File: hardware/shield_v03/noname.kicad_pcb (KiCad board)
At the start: 2 copper layers, 42 parts, among them J1 GS2, J2 GS2, J3 GS2, J4 Conn_02x05, J5 Conn_02x05, P1 V_IN, P2 PINZA_1, P3 PINZA_2, P4 PINZA_3, P5 PINZA_4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

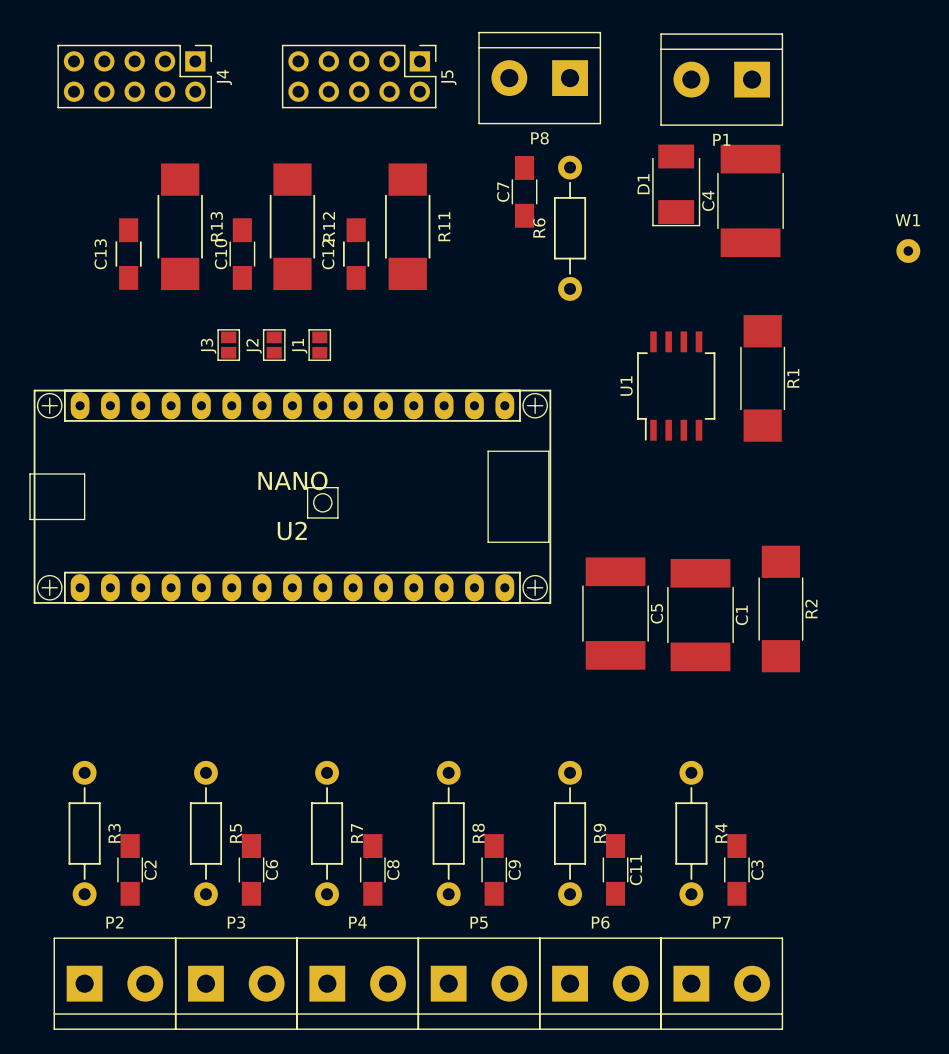
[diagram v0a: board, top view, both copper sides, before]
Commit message: hardware, rehubicacion de componentes
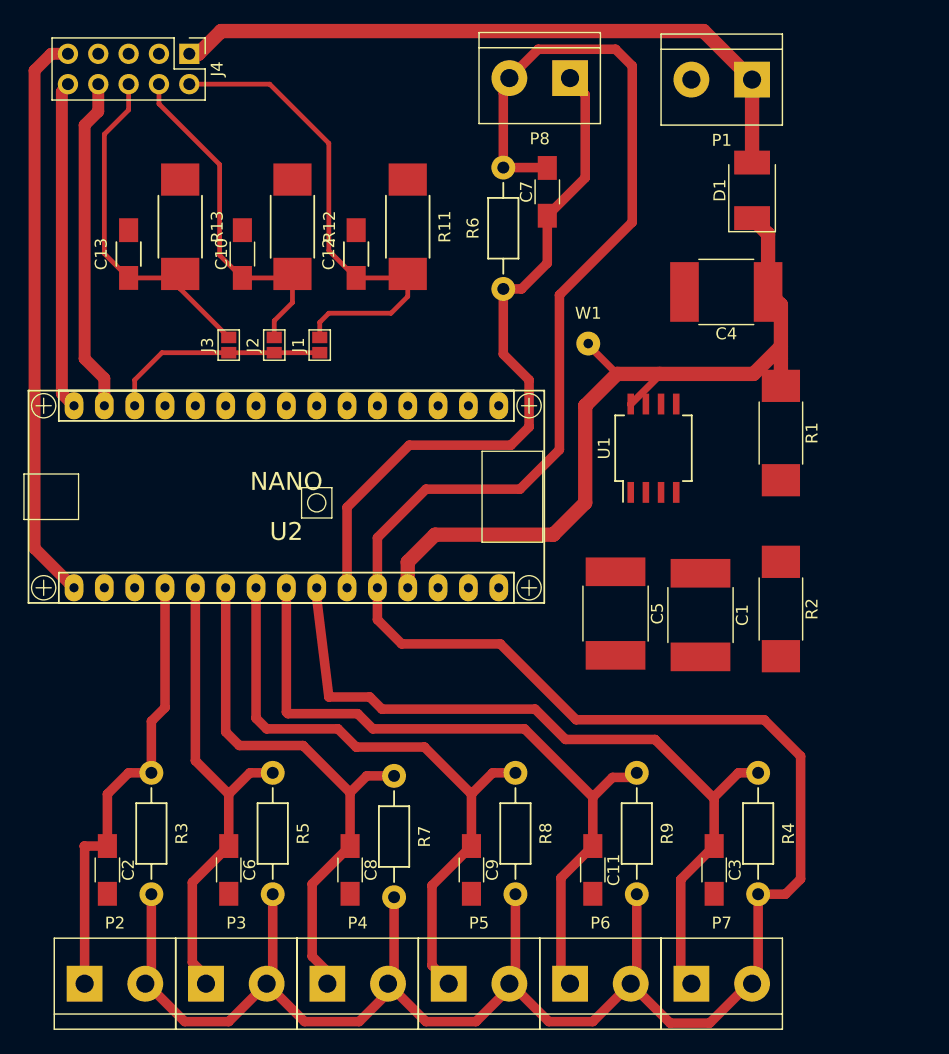
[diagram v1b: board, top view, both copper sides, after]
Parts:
- removed J5: Conn_02x05, oscar_libreria_huellas:Pin_Header_Straight_2x05_Pitch2.54mm_onsar
- J4: value Conn_02x05 -> Conn_02x05_Odd_Even; footprint oscar_libreria_huellas:Pin_Header_Straight_2x05_Pitch2.54mm_onsar -> Pin_Headers:Pin_Header_Straight_2x05_Pitch2.54mm
- moved W1 27.9 mm to (108.6, 101.3)
- moved C4 7.89 mm to (120.1, 97.0), turned to 180 degrees
- moved D1 6.37 mm to (122.3, 88.5)
- moved R7 5.62 mm to (92.3, 137.5)
- moved R6 5.59 mm to (101.5, 96.8)
- moved R8 5.59 mm to (102.5, 137.3)
- moved R3 5.59 mm to (72.0, 137.3)
- moved R4 5.59 mm to (122.8, 137.3)
- moved R5 5.59 mm to (82.2, 137.3)
- moved R9 5.59 mm to (112.6, 137.3)
- moved U1 5.54 mm to (114.0, 110.1)
- moved R1 4.82 mm to (124.7, 108.8)
- moved C11 1.91 mm to (109.0, 145.4)
- moved C2 1.91 mm to (68.3, 145.4)
- moved C3 1.91 mm to (119.1, 145.4)
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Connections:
- P1 pad 1: GND -> /vcc_5v
- P1 pad 2: /vcc_5v -> GND
- P2 pad 1: /v_referencia -> /intensidad_1
- P2 pad 2: /intensidad_1 -> /v_referencia
- P3 pad 1: /v_referencia -> /intensidad_2
- P3 pad 2: /intensidad_2 -> /v_referencia
- P4 pad 1: /v_referencia -> /intensidad_3
- P4 pad 2: /intensidad_3 -> /v_referencia
- P5 pad 1: /v_referencia -> /intensidad_4
- P5 pad 2: /intensidad_4 -> /v_referencia
- P6 pad 1: /v_referencia -> /intensidad_5
- P6 pad 2: /intensidad_5 -> /v_referencia
- P7 pad 1: /v_referencia -> /intensidad_6
- P7 pad 2: /intensidad_6 -> /v_referencia
- P8 pad 1: /v_referencia -> /intensidad_7
- P8 pad 2: /intensidad_7 -> /v_referencia
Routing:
- net /v_referencia: track 0.00 -> 249.2 mm
- net VCC: track 0.00 -> 68.0 mm
- net /intensidad_6: track 0.00 -> 66.8 mm
- net /intensidad_5: track 0.00 -> 60.6 mm
- net /intensidad_7: track 0.00 -> 59.1 mm
- net /vcc_5v: track 0.00 -> 56.5 mm
- net /intensidad_4: track 0.00 -> 54.8 mm
- net /sck: track 0.00 -> 48.0 mm
- net /intensidad_3: track 0.00 -> 46.7 mm
- net /esp_d2: track 0.00 -> 42.0 mm
- net /intensidad_2: track 0.00 -> 41.1 mm
- net /intensidad_1: track 0.00 -> 38.2 mm
- net /esp_d1: track 0.00 -> 29.4 mm
- net /esp_d0: track 0.00 -> 29.4 mm
- net /mosi: track 0.00 -> 28.5 mm
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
